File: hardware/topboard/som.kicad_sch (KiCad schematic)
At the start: 8 parts

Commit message: Add IMU
Signed-off-by: gatecat <gatecat@ds0.me>
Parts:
- added SW?: SW_DIP_x04, symbol Switch:SW_DIP_x04
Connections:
- net GND: now also SW?.1, SW?.2, SW?.3, SW?.4
- net PS_LED: now reaches SOM?.1D45 (MIO77)
- net at SOM?.1A27 (MODE0_C2M): now also SW?.8
- net at SOM?.1A28 (MODE1_C2M): now also SW?.7
- net at SOM?.1A29 (MODE2_C2M): now also SW?.6
- net at SOM?.1A30 (MODE3_C2M): now also SW?.5
- net PS_ERR_OUT: now reaches SOM?.1B24 (PS_ERROR_OUT_M2C)
- net PS_ERR_STAT: now reaches SOM?.1B25 (PS_ERROR_STATUS_M2C)
- net IMU_FSYNC: now reaches SOM?.2D56 (HDC03)
- net IMU_INT: now reaches SOM?.2D57 (HDC04)
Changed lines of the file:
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@@
 (kicad_sch (version 20210621) (generator eeschema)
   (paper "A2")
+  (junction (at 59.69 96.52) (diameter 0) (color 0 0 0 0))
+  (junction (at 59.69 99.06) (diameter 0) (color 0 0 0 0))
+  (junction (at 59.69 101.6) (diameter 0) (color 0 0 0 0))
   (junction (at 114.3 140.97) (diameter 0) (color 0 0 0 0))
   (junction (at 114.3 151.13) (diameter 0) (color 0 0 0 0))
@@
   (no_connect (at 269.24 106.68))
   (no_connect (at 345.44 86.36))
+  (wire (pts (xy 59.69 93.98) (xy 59.69 96.52))
+    (stroke (width 0) (type default) (color 0 0 0 0))
+  )
+  (wire (pts (xy 59.69 96.52) (xy 59.69 99.06))
+    (stroke (width 0) (type default) (color 0 0 0 0))
+  )
+  (wire (pts (xy 59.69 96.52) (xy 63.5 96.52))
+    (stroke (width 0) (type default) (color 0 0 0 0))
+  )
+  (wire (pts (xy 59.69 99.06) (xy 59.69 101.6))
+    (stroke (width 0) (type default) (color 0 0 0 0))
+  )
+  (wire (pts (xy 59.69 99.06) (xy 63.5 99.06))
+    (stroke (width 0) (type default) (color 0 0 0 0))
+  )
+  (wire (pts (xy 59.69 101.6) (xy 59.69 106.68))
+    (stroke (width 0) (type default) (color 0 0 0 0))
+  )
+  (wire (pts (xy 59.69 101.6) (xy 63.5 101.6))
+    (stroke (width 0) (type default) (color 0 0 0 0))
+  )
+  (wire (pts (xy 63.5 93.98) (xy 59.69 93.98))
+    (stroke (width 0) (type default) (color 0 0 0 0))
+  )
+  (wire (pts (xy 78.74 93.98) (xy 116.84 93.98))
+    (stroke (width 0) (type default) (color 0 0 0 0))
+  )
+  (wire (pts (xy 78.74 96.52) (xy 116.84 96.52))
+    (stroke (width 0) (type default) (color 0 0 0 0))
+  )
+  (wire (pts (xy 78.74 99.06) (xy 116.84 99.06))
+    (stroke (width 0) (type default) (color 0 0 0 0))
+  )
+  (wire (pts (xy 78.74 101.6) (xy 116.84 101.6))
+    (stroke (width 0) (type default) (color 0 0 0 0))
+  )
   (wire (pts (xy 101.6 81.28) (xy 116.84 81.28))
     (stroke (width 0) (type default) (color 0 0 0 0))
@@
     (stroke (width 0) (type default) (color 0 0 0 0))
   )
+  (wire (pts (xy 187.96 86.36) (xy 193.04 86.36))
+    (stroke (width 0) (type default) (color 0 0 0 0))
+  )
+  (wire (pts (xy 187.96 88.9) (xy 193.04 88.9))
+    (stroke (width 0) (type default) (color 0 0 0 0))
+  )
   (wire (pts (xy 187.96 91.44) (xy 193.04 91.44))
     (stroke (width 0) (type default) (color 0 0 0 0))
@@
     (stroke (width 0) (type default) (color 0 0 0 0))
   )
+  (wire (pts (xy 330.2 139.7) (xy 345.44 139.7))
+    (stroke (width 0) (type default) (color 0 0 0 0))
+  )
   (wire (pts (xy 330.2 149.86) (xy 345.44 149.86))
     (stroke (width 0) (type default) (color 0 0 0 0))
@@
     (stroke (width 0) (type default) (color 0 0 0 0))
   )
+  (wire (pts (xy 330.2 345.44) (xy 345.44 345.44))
+    (stroke (width 0) (type default) (color 0 0 0 0))
+  )
+  (wire (pts (xy 330.2 347.98) (xy 345.44 347.98))
+    (stroke (width 0) (type default) (color 0 0 0 0))
+  )
   (wire (pts (xy 340.36 29.21) (xy 342.9 29.21))
     (stroke (width 0) (type default) (color 0 0 0 0))
@@
     )
   )
+  (global_label "PS_ERR_OUT" (shape output) (at 187.96 86.36 180) (fields_autoplaced)
+    (effects (font (size 1.27 1.27)) (justify right))
+    (property "Intersheet References" "${INTERSHEET_REFS}" (id 0) (at 173.8145 86.2806 0)
+      (effects (font (size 1.27 1.27)) (justify right) hide)
+    )
+  )
+  (global_label "PS_ERR_STAT" (shape output) (at 187.96 88.9 180) (fields_autoplaced)
+    (effects (font (size 1.27 1.27)) (justify right))
+    (property "Intersheet References" "${INTERSHEET_REFS}" (id 0) (at 173.2098 88.8206 0)
+      (effects (font (size 1.27 1.27)) (justify right) hide)
+    )
+  )
   (global_label "POWEROFF" (shape input) (at 187.96 91.44 180) (fields_autoplaced)
     (effects (font (size 1.27 1.27)) (justify right))
@@
     )
   )
+  (global_label "PS_LED" (shape output) (at 330.2 139.7 180) (fields_autoplaced)
+    (effects (font (size 1.27 1.27)) (justify right))
+    (property "Intersheet References" "${INTERSHEET_REFS}" (id 0) (at 320.8926 139.6206 0)
+      (effects (font (size 1.27 1.27)) (justify right) hide)
+    )
+  )
   (global_label "GTR_RIGHT_C2M+" (shape input) (at 330.2 149.86 180) (fields_autoplaced)
     (effects (font (size 1.27 1.27)) (justify right))
@@
     )
   )
+  (global_label "IMU_FSYNC" (shape output) (at 330.2 345.44 180) (fields_autoplaced)
+    (effects (font (size 1.27 1.27)) (justify right))
+    (property "Intersheet References" "${INTERSHEET_REFS}" (id 0) (at 317.4455 345.3606 0)
+      (effects (font (size 1.27 1.27)) (justify right) hide)
+    )
+  )
+  (global_label "IMU_INT" (shape input) (at 330.2 347.98 180) (fields_autoplaced)
+    (effects (font (size 1.27 1.27)) (justify right))
+    (property "Intersheet References" "${INTERSHEET_REFS}" (id 0) (at 320.5298 347.9006 0)
+      (effects (font (size 1.27 1.27)) (justify right) hide)
+    )
+  )
   (global_label "DSI0A_D1+" (shape output) (at 340.36 35.56 180) (fields_autoplaced)
     (effects (font (size 1.27 1.27)) (justify right))
@@
     (pin "1")
   )
+  (symbol (lib_id "power:GND") (at 59.69 106.68 0) (unit 1)
+    (in_bom yes) (on_board yes) (fields_autoplaced)
+    (property "Reference" "#PWR?" (id 0) (at 59.69 113.03 0)
+      (effects (font (size 1.27 1.27)) hide)
+    )
+    (property "Value" "GND" (id 1) (at 59.69 111.2424 0))
+    (property "Footprint" "" (id 2) (at 59.69 106.68 0)
+      (effects (font (size 1.27 1.27)) hide)
+    )
+    (property "Datasheet" "" (id 3) (at 59.69 106.68 0)
+      (effects (font (size 1.27 1.27)) hide)
+    )
+    (pin "1")
+  )
   (symbol (lib_id "power:GND") (at 111.76 30.48 270) (unit 1)
     (in_bom yes) (on_board yes) (fields_autoplaced)
@@
     (pin "1")
   )
+  (symbol (lib_id "Switch:SW_DIP_x04") (at 71.12 99.06 0) (unit 1)
+    (in_bom yes) (on_board yes) (fields_autoplaced)
+    (property "Reference" "SW?" (id 0) (at 71.12 87.4735 0))
+    (property "Value" "SW_DIP_x04" (id 1) (at 71.12 90.2486 0))
+    (property "Footprint" "" (id 2) (at 71.12 99.06 0)
+      (effects (font (size 1.27 1.27)) hide)
+    )
+    (property "Datasheet" "~" (id 3) (at 71.12 99.06 0)
+      (effects (font (size 1.27 1.27)) hide)
+    )
+    (pin "1")
+    (pin "2")
+    (pin "3")
+    (pin "4")
+    (pin "5")
+    (pin "6")
+    (pin "7")
+    (pin "8")
+  )
   (symbol (lib_id "kria_k26:KRIA_K26") (at 137.16 25.4 0) (unit 1)

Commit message: Connecting some misc SoM IO
Signed-off-by: gatecat <gatecat@ds0.me>
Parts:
- added C? (x4): 100n, symbol Device:C_Small
- added C? (x2): 1µ, symbol Device:C_Small
- added C?: 10µ, symbol Device:C_Small
- added FB?: Ferrite_Bead_Small, symbol Device:Ferrite_Bead_Small
- added U?: CP3225-125.000-3.3-25-X-T-TR, Oscillator:Oscillator_SMD_IDT_JS6-6_5.0x3.2mm_P1.27mm, symbol Oscillator:XUX52
- added U?: CP3225-100.000-3.3-25-X-T-TR, Oscillator:Oscillator_SMD_IDT_JS6-6_5.0x3.2mm_P1.27mm, symbol Oscillator:XUX52
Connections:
- net GND: now also C?.2, C?.2, C?.2, U?.3 (GND), U?.3 (GND)
- net PCIE_REFCLK+: now reaches SOM?.1C47 (GTR_REFCLK0_C2M_P)
- net PCIE_REFCLK-: now reaches SOM?.1C48 (GTR_REFCLK0_C2M_N)
- net REFCLK100+: now reaches SOM?.1D53 (GTR_REFCLK2_C2M_P)
- net REFCLK100+: now also C?.2
- net REFCLK100-: now reaches SOM?.1D54 (GTR_REFCLK2_C2M_N)
- net REFCLK100-: now also C?.2
- net REFCLK125+: now reaches SOM?.1A51 (GTR_REFCLK3_C2M_P)
- net REFCLK125+: now also C?.2
- net REFCLK125-: now reaches SOM?.1A52 (GTR_REFCLK3_C2M_N)
- net REFCLK125-: now also C?.2
- net DP_AUX+: now reaches SOM?.2C32 (HPC11_P)
- net DP_AUX+: now also SOM?.2C35 (HPC12_P)
- net DP_AUX-: now reaches SOM?.2C33 (HPC11_N)
- net DP_AUX-: now also SOM?.2C36 (HPC12_N)
- net UDISP_PWR_EN: now reaches SOM?.2C47 (HDB07)
- net UDISP_SDA: now reaches SOM?.2C50 (HDB09)
- net UDISP_SCL: now reaches SOM?.2C51 (HDB10)
- net UDISP_~{RST}: now reaches SOM?.2C52 (HDB11)
- new net: C?.1, U?.5 (OUT2) (x2)
- new net: C?.1, U?.4 (OUT) (x2)
- new net +3V3PS: FB?.1
- new net 3V3_OSC: C?.1, C?.1, C?.1, FB?.2, U?.6 (VDD), U?.6 (VDD)
- no-connect marks 3 -> 5

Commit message: Fixing various top board issues
Signed-off-by: gatecat <gatecat@ds0.me>
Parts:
- added C10, C9: 100n, symbol Device:C_Small
- added C4: 1µ, symbol Device:C_Small
- added R1: 0R, symbol Device:R_Small
- added U3: AX3HAF1-135.0000T, Oscillator:Oscillator_SMD_IDT_JS6-6_5.0x3.2mm_P1.27mm, symbol Oscillator:XUX52
- gave numbers to parts that had none: 12
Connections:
- net +1V8PL: now also SOM1.2B59 (VCCO_HDB), SOM1.2B60 (VCCO_HDB)
- net 3V3_OSC: now also C4.1, U3.6 (VDD)
- net GND: now also C4.2, R1.1, U3.3 (GND)
- net LINK_LI1+: now reaches SOM1.2A32 (HPC19_P)
- net LINK_LI1-: now reaches SOM1.2A33 (HPC19_N)
- net LINK_LI0+: now reaches SOM1.2A35 (HPC14_P)
- net LINK_LI0-: now reaches SOM1.2A36 (HPC14_N)
- net LINK_LOCLK+: now reaches SOM1.2A38 (HPC15_CC_P)
- net LINK_LOCLK-: now reaches SOM1.2A39 (HPC15_CC_N)
- net at SOM1.1A1 (VCC_BATT): now also R1.2
- net LINK_RO1+: now reaches SOM1.2D27 (HPC09_P)
- net LINK_RO1-: now reaches SOM1.2D28 (HPC09_N)
- net FRONT_LCD_~{RST}: now reaches SOM1.2D46 (HDB02)
- net FRONT_LCD_TE: now reaches SOM1.2D50 (HDB05)
- net LINK_RO0+: now reaches SOM1.2C26 (HPC17_P)
- net LINK_RO0-: now reaches SOM1.2C27 (HPC17_N)
- net LINK_RICLK+: now reaches SOM1.2C29 (HPC10_CC_P)
- net LINK_RICLK-: now reaches SOM1.2C30 (HPC10_CC_N)
- net FRONT_LED0: now reaches SOM1.2C54 (HDC06)
- net FRONT_LED1: now reaches SOM1.2C55 (HDC07)
- net LINK_LO0+: now reaches SOM1.2B27 (HPC06_P)
- net LINK_LO0-: now reaches SOM1.2B28 (HPC06_N)
- net LINK_LO1+: now reaches SOM1.2B30 (HPC13_P)
- net LINK_LO1-: now reaches SOM1.2B31 (HPC13_N)
- net LINK_RI0+: now reaches SOM1.2B33 (HPC16_P)
- net LINK_RI0-: now reaches SOM1.2B34 (HPC16_N)
- net LINK_RI1+: now reaches SOM1.2B36 (HPC07_P)
- net LINK_RI1-: now reaches SOM1.2B37 (HPC07_N)
- net DP_REFCLK+ renamed REFCLK135+
- net REFCLK135+: now also C9.2
- net DP_REFCLK- renamed REFCLK135-
- net REFCLK135-: now also C10.2
- net I2C0_SCL: no longer names the net of SOM1.1B33 (MIO39)
- net I2C0_SDA: no longer names the net of SOM1.1B32 (MIO38)
- net PS_POR: no longer names the net of SOM1.1C15 (PS_POR_L)
- net PS_SRST renamed SYS_RESET
- new net: C9.1, U3.4 (OUT)
- new net: C10.1, U3.5 (OUT2)
- no-connect marks 5 -> 128

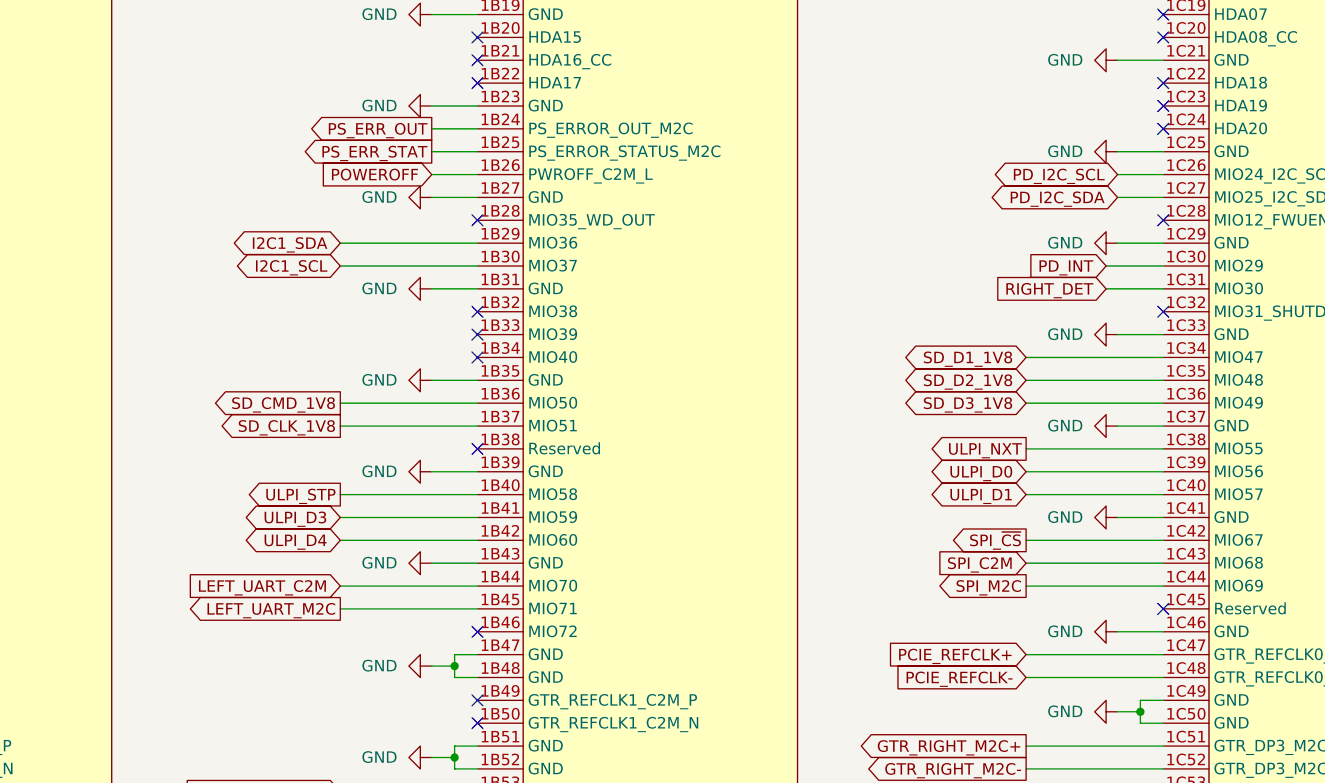
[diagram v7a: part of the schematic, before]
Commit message: Fix MPSoC pinout issues
Signed-off-by: gatecat <gatecat@ds0.me>
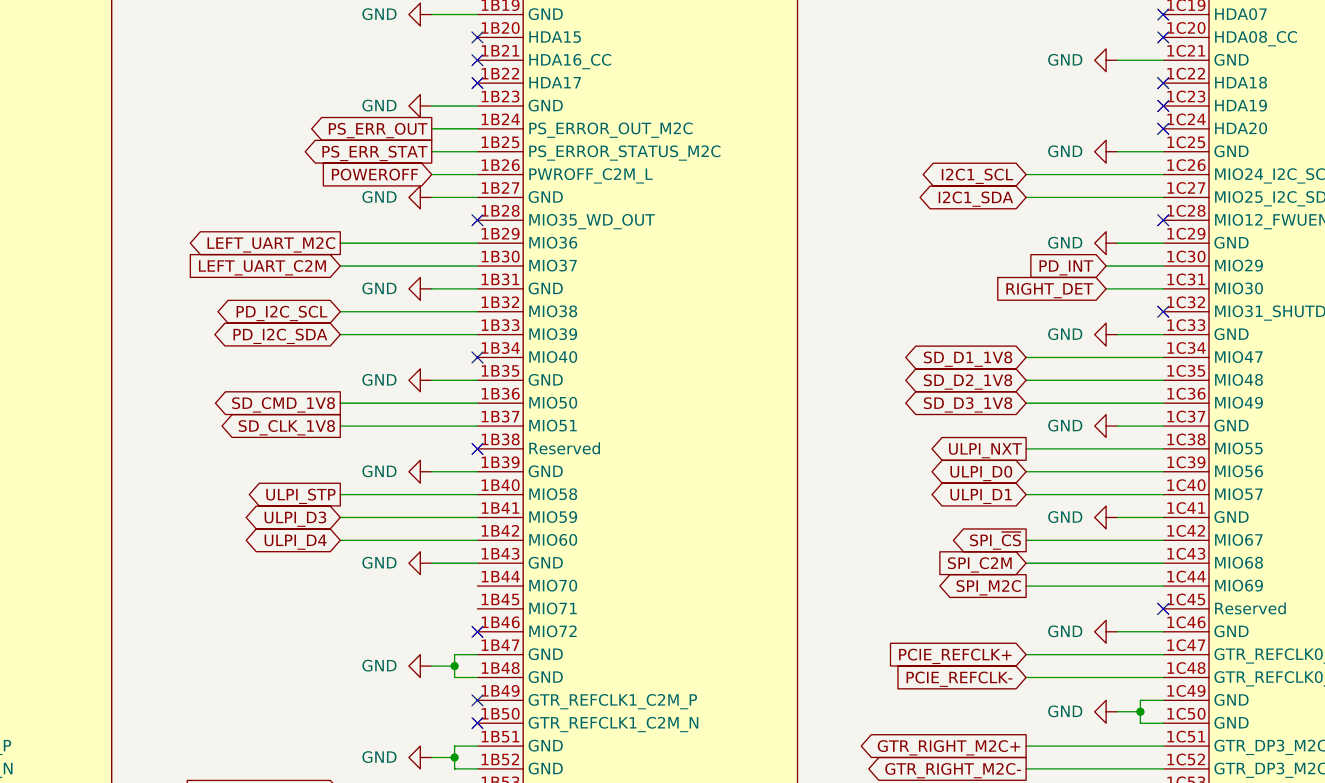
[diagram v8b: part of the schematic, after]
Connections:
- net I2C1_SCL: now also SOM1.1C26 (MIO24_I2C_SCK); no longer SOM1.1B30 (MIO37)
- net I2C1_SDA: now also SOM1.1C27 (MIO25_I2C_SDA); no longer SOM1.1B29 (MIO36)
- net LEFT_UART_C2M: now also SOM1.1B30 (MIO37); no longer SOM1.1B44 (MIO70)
- net LEFT_UART_M2C: now also SOM1.1B29 (MIO36); no longer SOM1.1B45 (MIO71)
- net PD_I2C_SCL: now also SOM1.1B32 (MIO38); no longer SOM1.1C26 (MIO24_I2C_SCK)
- net PD_I2C_SDA: now also SOM1.1B33 (MIO39); no longer SOM1.1C27 (MIO25_I2C_SDA)
- no-connect marks 128 -> 126
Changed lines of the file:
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@@
   (no_connect (at 193.04 81.28))
   (no_connect (at 193.04 96.52))
-  (no_connect (at 193.04 106.68))
-  (no_connect (at 193.04 109.22))
   (no_connect (at 193.04 111.76))
   (no_connect (at 193.04 121.92))
@@
     (stroke (width 0) (type default) (color 0 0 0 0))
   )
+  (wire (pts (xy 177.8 106.68) (xy 193.04 106.68))
+    (stroke (width 0) (type default) (color 0 0 0 0))
+  )
+  (wire (pts (xy 177.8 109.22) (xy 193.04 109.22))
+    (stroke (width 0) (type default) (color 0 0 0 0))
+  )
   (wire (pts (xy 177.8 116.84) (xy 193.04 116.84))
     (stroke (width 0) (type default) (color 0 0 0 0))
@@
     (stroke (width 0) (type default) (color 0 0 0 0))
   )
-  (wire (pts (xy 177.8 137.16) (xy 193.04 137.16))
-    (stroke (width 0) (type default) (color 0 0 0 0))
-  )
-  (wire (pts (xy 177.8 139.7) (xy 193.04 139.7))
-    (stroke (width 0) (type default) (color 0 0 0 0))
-  )
   (wire (pts (xy 177.8 160.02) (xy 193.04 160.02))
     (stroke (width 0) (type default) (color 0 0 0 0))
@@
     (stroke (width 0) (type default) (color 0 0 0 0))
   )
+  (wire (pts (xy 254 91.44) (xy 269.24 91.44))
+    (stroke (width 0) (type default) (color 0 0 0 0))
+  )
+  (wire (pts (xy 254 93.98) (xy 269.24 93.98))
+    (stroke (width 0) (type default) (color 0 0 0 0))
+  )
   (wire (pts (xy 254 111.76) (xy 269.24 111.76))
     (stroke (width 0) (type default) (color 0 0 0 0))
@@
     (stroke (width 0) (type default) (color 0 0 0 0))
   )
-  (wire (pts (xy 264.16 91.44) (xy 269.24 91.44))
-    (stroke (width 0) (type default) (color 0 0 0 0))
-  )
-  (wire (pts (xy 264.16 93.98) (xy 269.24 93.98))
-    (stroke (width 0) (type default) (color 0 0 0 0))
-  )
   (wire (pts (xy 264.16 99.06) (xy 269.24 99.06))
     (stroke (width 0) (type default) (color 0 0 0 0))
@@
     )
   )
-  (global_label "I2C1_SDA" (shape bidirectional) (at 177.8 99.06 180) (fields_autoplaced)
+  (global_label "LEFT_UART_M2C" (shape output) (at 177.8 99.06 180) (fields_autoplaced)
+    (effects (font (size 1.27 1.27)) (justify right))
+    (property "Intersheet References" "${INTERSHEET_REFS}" (id 0) (at 160.6307 98.9806 0)
+      (effects (font (size 1.27 1.27)) (justify right) hide)
+    )
+  )
+  (global_label "LEFT_UART_C2M" (shape input) (at 177.8 101.6 180) (fields_autoplaced)
+    (effects (font (size 1.27 1.27)) (justify right))
+    (property "Intersheet References" "${INTERSHEET_REFS}" (id 0) (at 160.6307 101.5206 0)
+      (effects (font (size 1.27 1.27)) (justify right) hide)
+    )
+  )
+  (global_label "PD_I2C_SCL" (shape bidirectional) (at 177.8 106.68 180) (fields_autoplaced)
     (effects (font (size 1.27 1.27)) (justify right))
-    (property "Intersheet References" "${INTERSHEET_REFS}" (id 0) (at 166.5574 98.9806 0)
+    (property "Intersheet References" "${INTERSHEET_REFS}" (id 0) (at 164.3198 106.6006 0)
       (effects (font (size 1.27 1.27)) (justify right) hide)
     )
   )
-  (global_label "I2C1_SCL" (shape bidirectional) (at 177.8 101.6 180) (fields_autoplaced)
+  (global_label "PD_I2C_SDA" (shape bidirectional) (at 177.8 109.22 180) (fields_autoplaced)
     (effects (font (size 1.27 1.27)) (justify right))
-    (property "Intersheet References" "${INTERSHEET_REFS}" (id 0) (at 166.6179 101.5206 0)
+    (property "Intersheet References" "${INTERSHEET_REFS}" (id 0) (at 164.2593 109.1406 0)
       (effects (font (size 1.27 1.27)) (justify right) hide)
     )
@@
     )
   )
-  (global_label "LEFT_UART_C2M" (shape input) (at 177.8 137.16 180) (fields_autoplaced)
-    (effects (font (size 1.27 1.27)) (justify right))
-    (property "Intersheet References" "${INTERSHEET_REFS}" (id 0) (at 160.6307 137.0806 0)
-      (effects (font (size 1.27 1.27)) (justify right) hide)
-    )
-  )
-  (global_label "LEFT_UART_M2C" (shape output) (at 177.8 139.7 180) (fields_autoplaced)
-    (effects (font (size 1.27 1.27)) (justify right))
-    (property "Intersheet References" "${INTERSHEET_REFS}" (id 0) (at 160.6307 139.6206 0)
-      (effects (font (size 1.27 1.27)) (justify right) hide)
-    )
-  )
   (global_label "GTR_LEFT_C2M+" (shape input) (at 177.8 160.02 180) (fields_autoplaced)
     (effects (font (size 1.27 1.27)) (justify right))
@@
     )
   )
+  (global_label "I2C1_SCL" (shape bidirectional) (at 254 91.44 180) (fields_autoplaced)
+    (effects (font (size 1.27 1.27)) (justify right))
+    (property "Intersheet References" "${INTERSHEET_REFS}" (id 0) (at 242.8179 91.5194 0)
+      (effects (font (size 1.27 1.27)) (justify right) hide)
+    )
+  )
+  (global_label "I2C1_SDA" (shape bidirectional) (at 254 93.98 180) (fields_autoplaced)
+    (effects (font (size 1.27 1.27)) (justify right))
+    (property "Intersheet References" "${INTERSHEET_REFS}" (id 0) (at 242.7574 94.0594 0)
+      (effects (font (size 1.27 1.27)) (justify right) hide)
+    )
+  )
   (global_label "SD_D1_1V8" (shape bidirectional) (at 254 111.76 180) (fields_autoplaced)
     (effects (font (size 1.27 1.27)) (justify right))
@@
     )
   )
-  (global_label "PD_I2C_SCL" (shape bidirectional) (at 264.16 91.44 180) (fields_autoplaced)
-    (effects (font (size 1.27 1.27)) (justify right))
-    (property "Intersheet References" "${INTERSHEET_REFS}" (id 0) (at 250.6798 91.3606 0)
-      (effects (font (size 1.27 1.27)) (justify right) hide)
-    )
-  )
-  (global_label "PD_I2C_SDA" (shape bidirectional) (at 264.16 93.98 180) (fields_autoplaced)
-    (effects (font (size 1.27 1.27)) (justify right))
-    (property "Intersheet References" "${INTERSHEET_REFS}" (id 0) (at 250.6193 93.9006 0)
-      (effects (font (size 1.27 1.27)) (justify right) hide)
-    )
-  )
   (global_label "RECOVERY" (shape input) (at 330.2 101.6 180) (fields_autoplaced)
     (effects (font (size 1.27 1.27)) (justify right))
@@
   )
   (symbol (lib_id "power:GND") (at 187.96 114.3 270) (unit 1)
-    (in_bom yes) (on_board yes) (fields_autoplaced)
+    (in_bom yes) (on_board yes)
     (property "Reference" "#PWR0142" (id 0) (at 181.61 114.3 0)
       (effects (font (size 1.27 1.27)) hide)
